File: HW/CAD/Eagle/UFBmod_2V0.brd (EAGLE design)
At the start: 98.4 x 89.5 mm, 196 parts, among them T0551 MMBT2222, U0501 MIDAS_MCCOG21605B6W-FPTLWI, U0601 MAX5217, U0701 AT86RF215-ZU, U0711 ASVTX-13-D-26.000MHZ-I05-T, U0811 PE4259, U0821 RFX1010, U0881 B39871B3440U410, U0911 FT232HL, U1101 TPS53353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

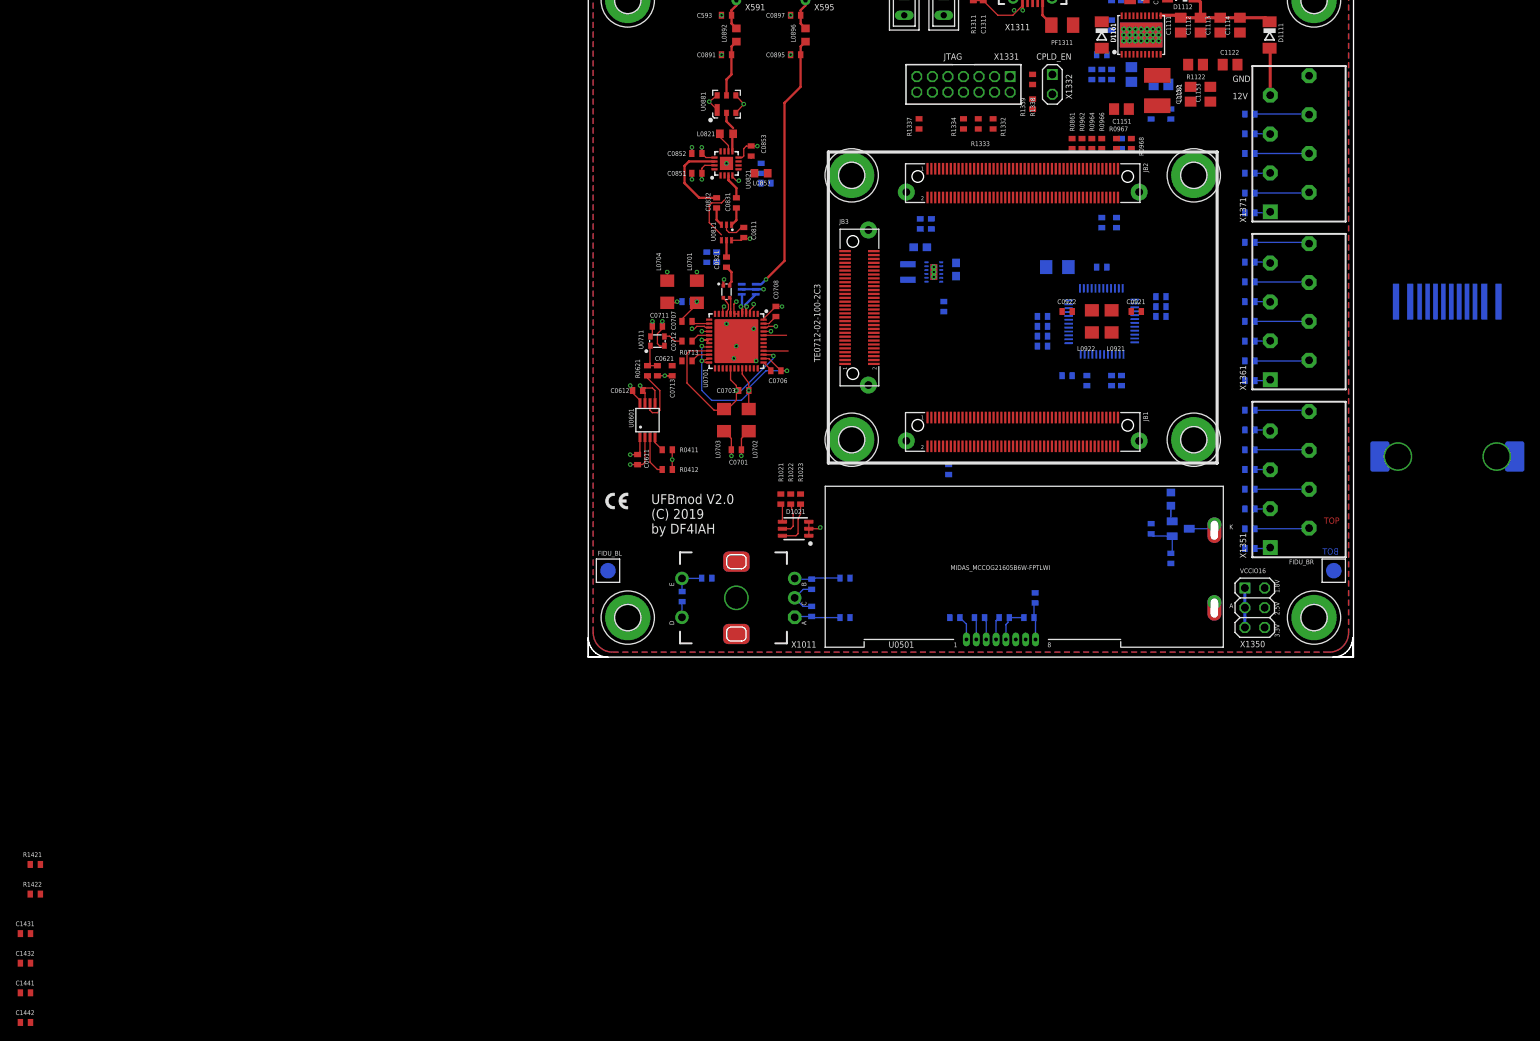
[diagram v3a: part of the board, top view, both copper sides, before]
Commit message: HW_2V0 - HW/CAD/Eagle - ARJE-0034 placed
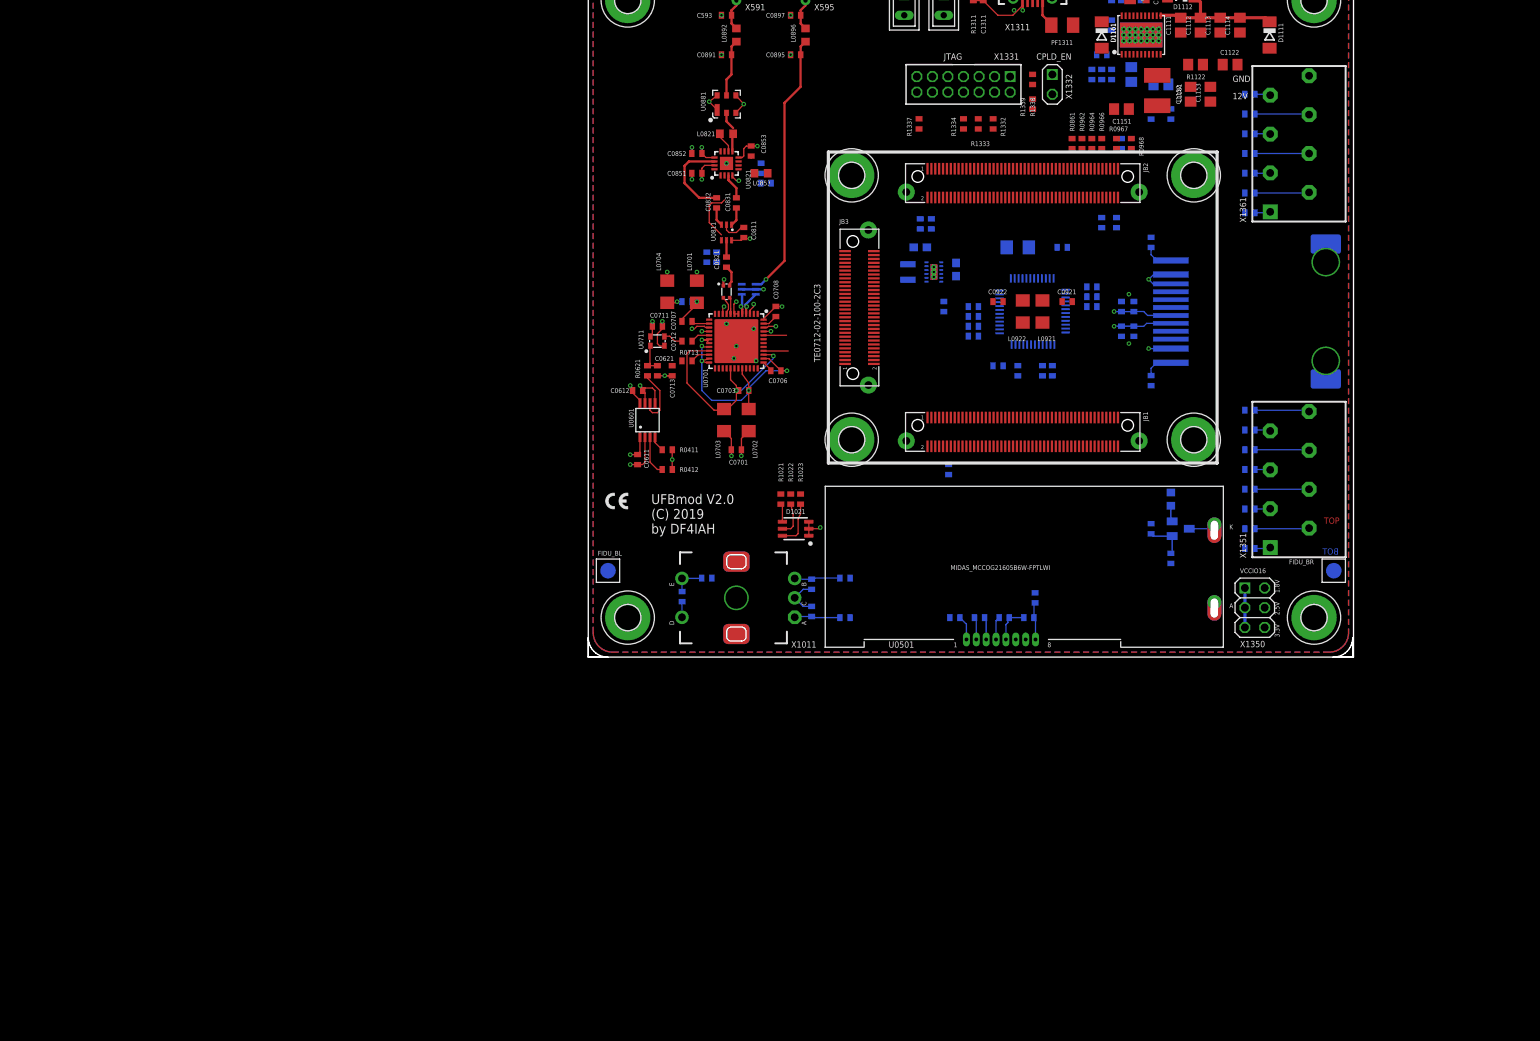
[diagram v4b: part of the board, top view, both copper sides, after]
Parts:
- removed R1368, R1371, R1372, R1373, R1374, R1375, R1376: 100R, df4iah_rcl:R0402
- removed X1371: PHOENIX_1990067_1X8X2MM50_PTSA-0-5, df4iah_connector:PHOENIX_1990067_1X8X2MM50_PTSA-0-5
- moved C1442 169.7 mm to (70.2, 45.1), flipped to the bottom, turned to 90 degrees
- moved C1441 166.3 mm to (68.6, 45.1), flipped to the bottom, turned to 90 degrees
- moved R1422 166.2 mm to (72.4, 53.3), flipped to the bottom, turned to 270 degrees
- moved C1432 164.1 mm to (70.2, 41.9), flipped to the bottom, turned to 270 degrees
- moved C1431 160.9 mm to (68.6, 41.9), flipped to the bottom, turned to 270 degrees
- moved R1421 156.4 mm to (72.4, 35.6), flipped to the bottom, turned to 90 degrees
- moved J1411 26.2 mm to (86.4, 44.5), turned to 270 degrees
- moved R1365 21.6 mm to (85.1, 67.3)
- moved R1367 21.6 mm to (85.1, 72.4)
- moved R1361 21.6 mm to (85.1, 57.1)
- moved R1362 21.6 mm to (85.1, 59.7)
- moved R1363 21.6 mm to (85.1, 62.2)
- moved R1364 21.6 mm to (85.1, 64.8)
- moved R1366 21.6 mm to (85.1, 69.8)
- moved X1361 21.6 mm to (92.7, 64.8)
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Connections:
- removed net B2W_68: R1368.2, X1361.8
- removed net B2W_71: R1371.2, X1371.1
- removed net B2W_72: R1372.2, X1371.2
- removed net B2W_73: R1373.2, X1371.3
- removed net B2W_74: R1374.2, X1371.4
- removed net B2W_75: R1375.2, X1371.5
- removed net B2W_76: R1376.2, X1371.6
- net FPGA_B16_L10_N: no longer R1368.1
- net FPGA_B16_L2_N: no longer R1374.1
- net FPGA_B16_L2_P: no longer R1373.1
- net FPGA_B16_L5_N: no longer R1372.1
- net FPGA_B16_L5_P: no longer R1371.1
- net FPGA_B16_L6_N: no longer R1376.1
- net FPGA_B16_L6_P: no longer R1375.1
- net GND: now also X1361.8; no longer X1371.8
- net VIN_PWR: no longer X1371.7
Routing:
- net +3V3: track 30.3 -> 45.3 mm, vias 9 -> 11
- net GND: track 82.6 -> 91.7 mm, vias 34 -> 38
- net B2W_68: track 7.13 -> 0.00 mm
- net B2W_72: track 7.05 -> 0.00 mm
- net B2W_76: track 7.05 -> 0.00 mm
- net B2W_74: track 6.97 -> 0.00 mm
- net VIN_PWR: track 6.12 -> 0.08 mm
- net ETH_DA_G: track 0.00 -> 3.78 mm
- net ETH_DA_Y: track 0.00 -> 3.77 mm
- net B2W_71: track 2.09 -> 0.00 mm
- net B2W_75: track 2.01 -> 0.00 mm
- net B2W_73: track 2.01 -> 0.00 mm

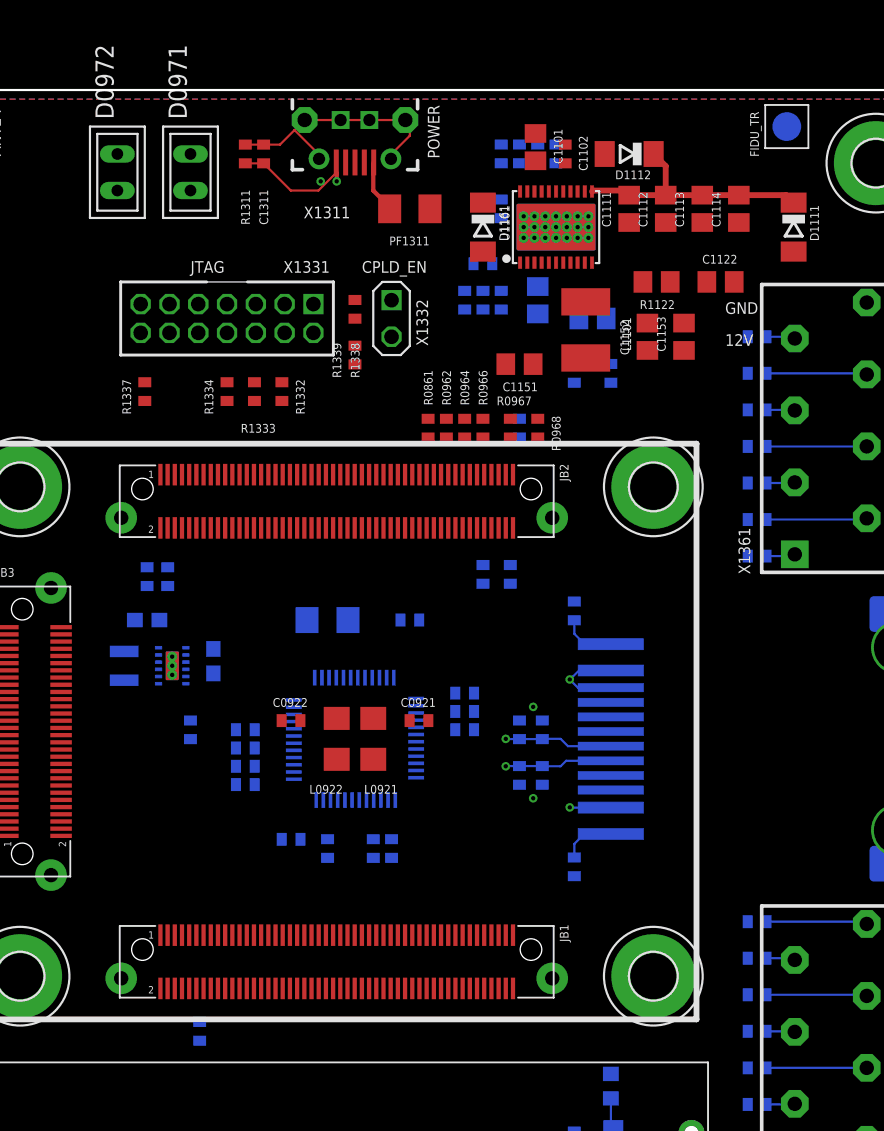
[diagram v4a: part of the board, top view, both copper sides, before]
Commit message: HW_2V0 - HW/CAD/Eagle - routing of PMIC 3.3V done
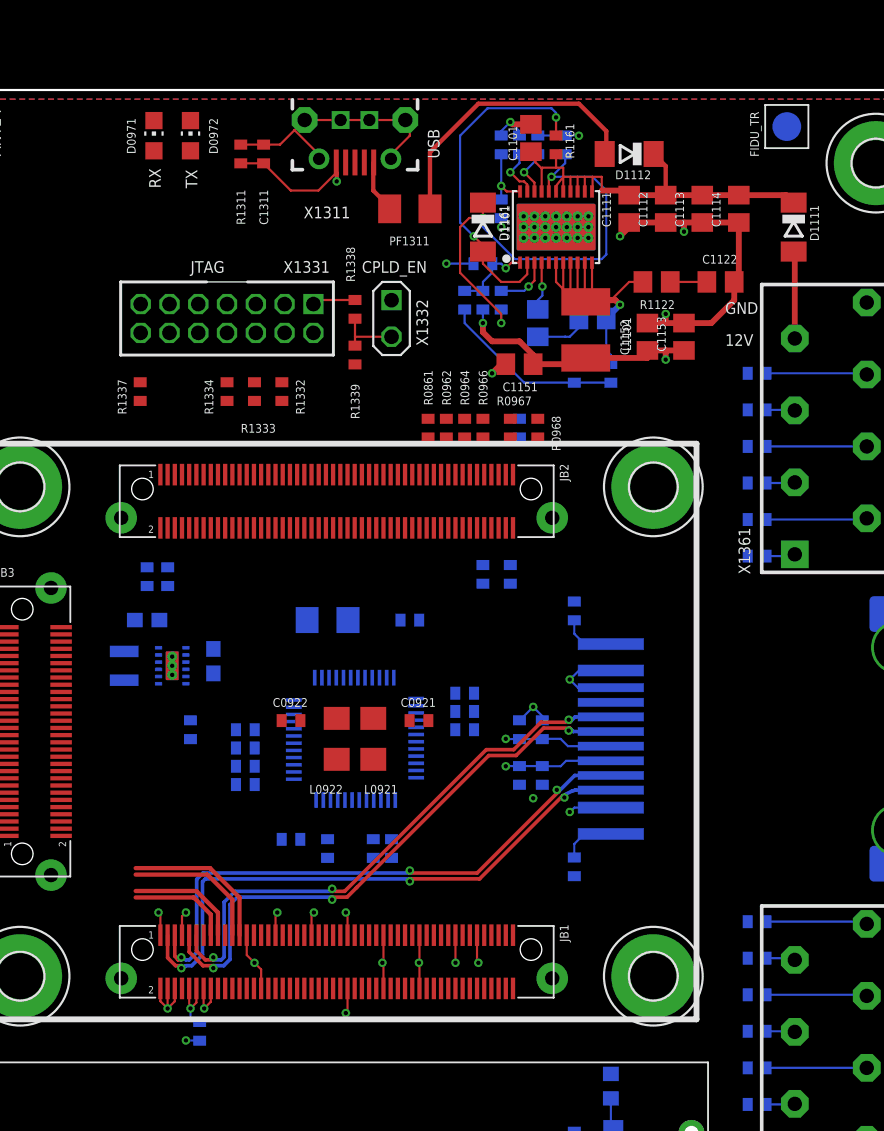
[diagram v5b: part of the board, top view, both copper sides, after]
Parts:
- removed R1367: 100R, df4iah_rcl:R0402
- D0971: value GREEN -> CMD17-21VGD/TR8 GREEN; device df4iah_led:U57X32 -> df4iah_led:CHIP-LED0805
- D0972: value RED -> CMD17-21VRD/TR8 RED; device df4iah_led:U57X32 -> df4iah_led:CHIP-LED0805
- moved D0972 5.68 mm to (45.7, 86.4), turned to 0 degrees
- moved D0971 3.59 mm to (43.2, 86.4), turned to 0 degrees
- moved R1108 1.59 mm to (69.8, 73.3)
- moved C1101 0.71 mm to (69.4, 86.2)
- moved C1102 0.63 mm to (71.8, 85.7), flipped to the bottom
- moved R1103 0.63 mm to (67.3, 85.7)
- moved R1105 0.63 mm to (68.6, 85.7)
- moved R1106 0.63 mm to (69.8, 85.7)
- moved R1161 0.63 mm to (71.1, 85.7), flipped to the top
- moved R1311 0.32 mm to (49.2, 85.1)
- moved R1337 0.32 mm to (42.2, 68.6)
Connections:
- removed net B2W_67: R1367.2, X1361.7
- net FPGA_B16_L10_P: no longer R1367.1
- net GND: now also D0971.C, D0972.C; no longer D0971.K, D0972.K
- net VIN_PWR: now also X1361.7
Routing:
- net GND: track 91.7 -> 158.9 mm, vias 38 -> 56
- net FPGA_ETH_TD_P: track 0.00 -> 41.5 mm, vias 0 -> 3
- net FPGA_ETH_RD_P: track 0.00 -> 41.1 mm, vias 0 -> 3
- net FPGA_ETH_TD_N: track 0.00 -> 41.1 mm, vias 0 -> 3
- net FPGA_ETH_RD_N: track 0.00 -> 40.4 mm, vias 0 -> 3
- net TPS_VREG: track 0.00 -> 33.7 mm, vias 0 -> 3
- net TPS_LL: track 0.00 -> 31.2 mm, vias 0 -> 1
- net +3V3: track 45.3 -> 71.9 mm, vias 11 -> 16
- net TPS_EN: track 0.00 -> 23.3 mm, vias 0 -> 2
- net +5V_USB: track 0.00 -> 20.0 mm
- net TPS_VIN: track 17.6 -> 32.8 mm
- net TPS_COR: track 0.00 -> 12.8 mm
- net TRX_TXD_P: track 0.00 -> 10.7 mm
- net TRX_TXD_N: track 0.00 -> 9.91 mm
- net TRX_TXCLK_P: track 0.00 -> 7.91 mm
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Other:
- board text added: "RX"
- board text added: "TX"
- board text added: "USB"
- board text removed: "POWER"

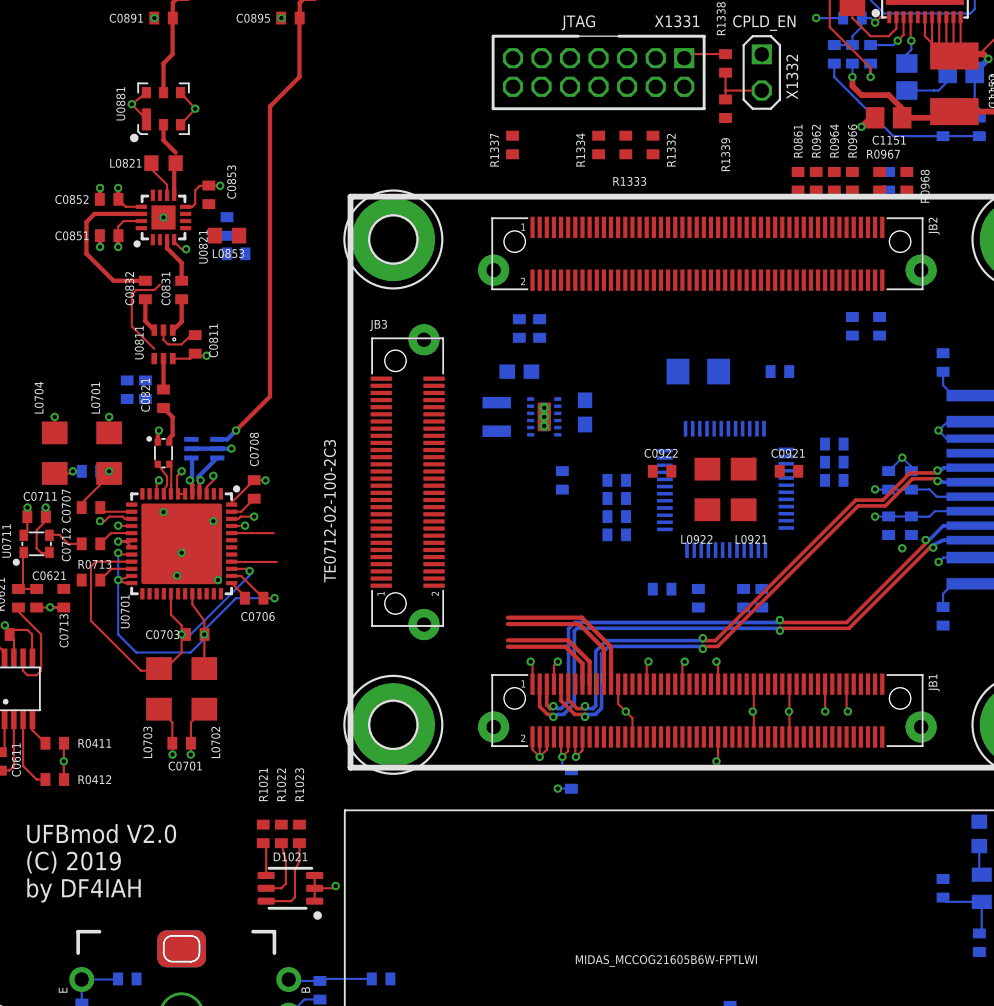
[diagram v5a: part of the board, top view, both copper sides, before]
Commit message: HW_2V0 - HW/CAD/Eagle - LVDS traces to TRX added
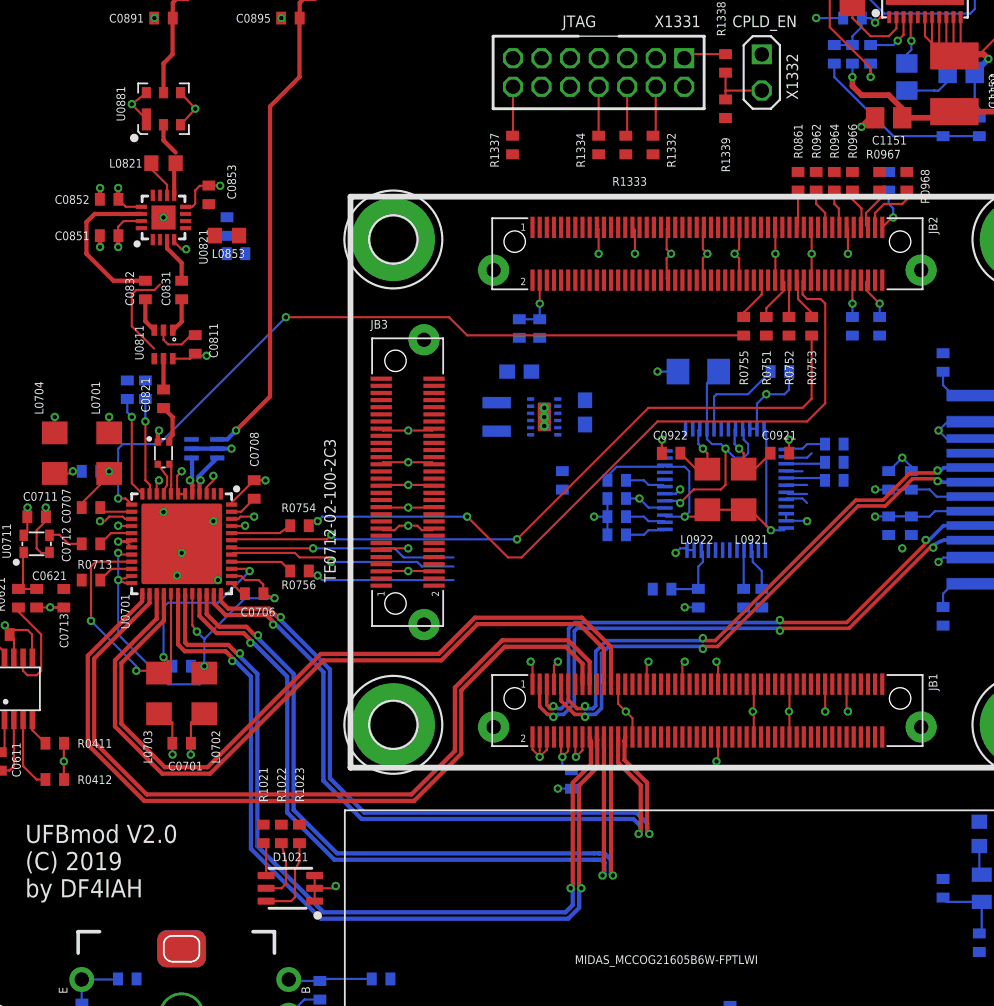
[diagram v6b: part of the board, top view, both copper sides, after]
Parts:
- added R0751, R0752, R0753, R0754, R0755, R0756: 100R, df4iah_rcl:R0402
- moved C0703 2.42 mm to (19.1, 32.1), flipped to the bottom, turned to 180 degrees
- moved C0922 1.42 mm to (53.3, 47.0)
- moved C0921 1.42 mm to (61.0, 47.0)
- moved C0706 0.32 mm to (24.1, 37.1)
- moved L0702 0.32 mm to (20.6, 30.2)
- moved L0703 0.32 mm to (17.5, 30.2)
- turned R0961 to 180 degrees
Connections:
- new net TRX_IRQ_R: R0756.1, U0701.40
- new net TRX_MISO_R: R0754.1, U0701.44
- new net TRX_MOSI_R: R0753.1, U0701.43
- new net TRX_RSTN_R: R0755.1, U0701.13
- new net TRX_SCLK_R: R0751.1, U0701.41
- new net TRX_SELN_R: R0752.1, U0701.42
- net TRX_IRQ: now also JB2.68, R0756.2; no longer U0701.40
- net TRX_MISO: now also JB2.78, R0754.2; no longer U0701.44
- net TRX_MOSI: now also JB2.76, R0753.2; no longer U0701.43
- net TRX_RSTN: now also JB2.66, R0755.2; no longer U0701.13
- net TRX_SCLK: now also JB2.72, R0751.2; no longer U0701.41
- net TRX_SELN: now also JB2.74, R0752.2; no longer U0701.42
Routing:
- net GND: track 158.9 -> 228.8 mm, vias 56 -> 80
- net TRX_RXD09_N: track 0.00 -> 60.1 mm, vias 0 -> 2
- net TRX_RXD09_P: track 0.00 -> 58.6 mm, vias 0 -> 2
- net TRX_RXCLK_N: track 0.00 -> 53.8 mm, vias 0 -> 2
- net TRX_RXCLK_P: track 0.00 -> 53.7 mm, vias 0 -> 2
- net TRX_RSTN_R: track 0.00 -> 52.8 mm, vias 0 -> 2
- net TRX_TXCLK_N: track 7.15 -> 57.4 mm
- net TRX_RXD24_N: track 0.00 -> 50.1 mm, vias 0 -> 2
- net TRX_RXD24_P: track 0.00 -> 50.1 mm, vias 0 -> 2
- net TRX_TXCLK_P: track 7.91 -> 57.5 mm
- net TRX_MOSI_R: track 0.00 -> 49.4 mm, vias 0 -> 2
- net TRX_MISO: track 2.95 -> 52.0 mm, vias 0 -> 2
- net TRX_TXD_N: track 9.91 -> 53.7 mm
- net TRX_TXD_P: track 10.7 -> 53.7 mm
- net FT_VCCD: track 0.00 -> 26.5 mm, vias 0 -> 2
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
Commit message: HW - CAD/Eagle - RGB-LED and LCD backlight connected
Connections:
- net FPGA_LCD_BL_PWM: now also JB1.84
- net FPGA_LED_RGB_BLUE: now also JB1.36
- net FPGA_LED_RGB_GREEN: now also JB1.34
- net FPGA_LED_RGB_RED: now also JB1.32
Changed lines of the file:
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@@
 <signal name="FPGA_LED_RGB_GREEN">
 <contactref element="R1022" pad="2"/>
+<contactref element="JB1" pad="34"/>
+<wire x1="26.035" y1="20.97" x2="51.63" y2="27.11" width="0" layer="19" extent="1-1"/>
 </signal>
 <signal name="FPGA_LED_RGB_BLUE">
 <contactref element="R1023" pad="2"/>
+<contactref element="JB1" pad="36"/>
+<wire x1="27.305" y1="20.97" x2="52.13" y2="27.11" width="0" layer="19" extent="1-1"/>
 </signal>
 <signal name="LED_RGB_RED">
@@
 <signal name="FPGA_LED_RGB_RED">
 <contactref element="R1021" pad="2"/>
+<contactref element="JB1" pad="32"/>
+<wire x1="24.765" y1="20.97" x2="51.13" y2="27.11" width="0" layer="19" extent="1-1"/>
 </signal>
 <signal name="ROT_P">
@@
 <signal name="FPGA_LCD_BL_PWM">
 <contactref element="R0552" pad="2"/>
+<contactref element="JB1" pad="84"/>
+<wire x1="72.39" y1="17.16" x2="64.13" y2="27.11" width="0" layer="19" extent="1-16"/>
 </signal>
 <signal name="+5V_USB">
